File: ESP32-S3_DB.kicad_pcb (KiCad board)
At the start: 2 copper layers, 117 parts, among them CN1 JST_Battery, IC1 MAX485ESA+T, IC2 ATA6561-GAQW-N, J1 TYPE-C-31-M12_13, J10 Conn_01x16_Socket, J2 A - B, J3 H - L, J4 TYPE-C-31-M12_13, J5 EXT_LOAD, J6 R4_TX, J7 R4_RX, J8 Micro_SD_Card_Det1, J9 Conn_01x16_Socket, Q1 NMOS, Q2 NMOS, SW1 RESET, SW2 BOOT, SW3 ON/OFF, U1 ESP32-S3FH4R2, U3 IP5306, U4 CH340X, U5 AP2127N-3.3TRG1, X1 32.768KHz, Y1 40MHz

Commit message: Arranged power section on PCB
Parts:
- added D1: BLUE, ESP32-S3_Dev_Board:LED_0603_1608Metric, F.Cu at (160.5, 113.9)
- added R8: 0E, ESP32-S3_Dev_Board:R_0603_1608Metric, F.Cu at (150.2, 101.7)
- moved J4 329.5 mm to (170.6, 110.4), turned to 90 degrees
- moved R5 319.4 mm to (165.8, 94.0), turned to 90 degrees
- moved D11 313.2 mm to (164.0, 110.2), turned to 90 degrees
- moved D7 312.9 mm to (151.9, 120.7)
- moved R7 312.9 mm to (166.5, 107.8), turned to 90 degrees
- moved D3 312.6 mm to (151.8, 122.4), turned to 180 degrees
- moved R6 311.9 mm to (164.4, 112.5), turned to 180 degrees
- moved D9 311.2 mm to (151.8, 117.2)
- moved D8 311.0 mm to (151.8, 119.0), turned to 180 degrees
- moved R39 309.0 mm to (157.5, 114.0)
- moved R16 302.4 mm to (145.1, 126.2)
- moved R15 302.1 mm to (146.4, 104.4), turned to -90 degrees
- moved C10 296.3 mm to (146.0, 117.5)
- moved L4 295.6 mm to (139.6, 123.3), turned to 180 degrees
- moved R9 294.3 mm to (140.9, 116.8), turned to 180 degrees
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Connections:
- D2 pad 4: /INPUT POWER/5V -> /5V
- J1 pad A4: /INPUT POWER/5V -> /INPUT POWER/VIN
- J1 pad B4: /INPUT POWER/5V -> /INPUT POWER/VIN
- R15 pad 1: /INPUT POWER/5V -> /INPUT POWER/VIN
- R9 pad 1: /INPUT POWER/5V -> /INPUT POWER/VIN

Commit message: Added bulk Decoupling and arranged components
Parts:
- added C1: 22uF, ESP32-S3_Dev_Board:C_1206_3216Metric, F.Cu at (111.8, 120.4)
- added C37: 22uF, ESP32-S3_Dev_Board:C_1206_3216Metric, F.Cu at (111.8, 123.8)
- added C38: 22uF, ESP32-S3_Dev_Board:C_1206_3216Metric, F.Cu at (111.8, 127.1)
- added C39: 22uF, ESP32-S3_Dev_Board:C_1206_3216Metric, F.Cu at (111.8, 130.5)
- added R45: 10E, ESP32-S3_Dev_Board:R_0402_1005Metric, F.Cu at (131.6, 99.9)
- added R46: 10E, ESP32-S3_Dev_Board:R_0402_1005Metric, F.Cu at (135.2, 102.0)
- added R47: 10E, ESP32-S3_Dev_Board:R_0402_1005Metric, F.Cu at (-94.0, 66.7)
- added R48: 10E, ESP32-S3_Dev_Board:R_0402_1005Metric, F.Cu at (-94.0, 68.7)
- added R49: 10E, ESP32-S3_Dev_Board:R_0402_1005Metric, F.Cu at (-98.9, 66.7)
- added R50: 10E, ESP32-S3_Dev_Board:R_0402_1005Metric, F.Cu at (-98.9, 68.7)
- added R51: 10E, ESP32-S3_Dev_Board:R_0402_1005Metric, F.Cu at (-98.9, 70.7)
- added R52: 10E, ESP32-S3_Dev_Board:R_0402_1005Metric, F.Cu at (-98.9, 72.7)
- added R53: 10E, ESP32-S3_Dev_Board:R_0402_1005Metric, F.Cu at (-98.9, 74.7)
- added R54: 10E, ESP32-S3_Dev_Board:R_0402_1005Metric, F.Cu at (-98.9, 76.7)
- moved R26 311.1 mm to (167.2, 90.2), turned to 180 degrees
- moved R27 307.4 mm to (163.8, 90.3)
- moved J7 306.8 mm to (170.6, 73.9)
- moved J6 304.7 mm to (164.2, 74.1)
- moved J3 296.0 mm to (169.9, 121.9), turned to 180 degrees
- moved J2 291.8 mm to (170.0, 85.2)
- moved J8 286.6 mm to (151.3, 83.7)
- moved C20 282.9 mm to (153.7, 106.4), turned to 180 degrees
- moved C19 281.9 mm to (153.6, 111.4), turned to 180 degrees
- moved D10 280.8 mm to (138.6, 84.0)
- moved CN1 279.1 mm to (135.9, 127.8), turned to 180 degrees
- moved J5 276.4 mm to (129.7, 82.3)
- moved R20 272.5 mm to (149.4, 107.8)
- moved R43 272.1 mm to (144.3, 109.0)
- moved R44 269.6 mm to (144.5, 113.7)
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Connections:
- D13 pad 2: /BOOT_TXD -> Net-(D13-A)
- J1 pad A6: /D+ -> Net-(J1-D+-PadA6)
- J1 pad A7: /D- -> Net-(J1-D--PadA7)
- J1 pad B6: /D+ -> Net-(J1-D+-PadA6)
- J1 pad B7: /D- -> Net-(J1-D--PadA7)
- U1 pad 15: /SD_~{CS} -> Net-(U1-GPIO10)
- U1 pad 16: /SD_MOSI -> Net-(U1-GPIO11)
- U1 pad 17: /SD_CLK -> Net-(U1-GPIO12)
- U1 pad 18: /SD_MISO -> Net-(U1-GPIO13)
- U1 pad 25: /OTG_D- -> /ESP32-S3-MCU/D-
- U1 pad 26: /OTG_D+ -> /ESP32-S3-MCU/D+
- U4 pad 8: /BOOT_RXD -> Net-(U4-TXD)
- U4 pad 9: /BOOT_TXD -> Net-(D13-A)

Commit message: Changed USB C footprint and arranged components
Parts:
- added C40: 10uF, ESP32-S3_Dev_Board:C_0805_2012Metric, F.Cu at (202.4, 106.7)
- added C41: 1uF, ESP32-S3_Dev_Board:C_0603_1608Metric, F.Cu at (204.6, 106.7)
- J1, J4: footprint ESP32-S3_Dev_Board:USB-C_SMD-TYPE-C-31-M-12 -> ESP32-S3_Dev_Board:tyye_c_connector
- moved J9 301.7 mm to (131.2, 136.3), turned to -90 degrees
- moved R47 301.1 mm to (203.9, 110.5), turned to 180 degrees
- moved R48 301.0 mm to (203.9, 112.0), turned to 180 degrees
- moved J10 257.6 mm to (91.9, 138.8), turned to 90 degrees
- moved J6 66.4 mm to (230.5, 77.8)
- moved J2 62.8 mm to (230.8, 69.4)
- moved J8 60.7 mm to (210.7, 71.0)
- moved J3 56.8 mm to (192.3, 69.7), turned to 0 degrees
- moved J7 54.6 mm to (225.1, 77.8)
- moved J5 49.6 mm to (177.7, 69.8)
- moved J1 43.3 mm to (211.7, 110.5)
- moved J4 43.0 mm to (211.8, 122.8)
- moved R4 42.6 mm to (204.3, 113.7), turned to -90 degrees
- moved D11 41.8 mm to (203.8, 122.9)
- moved D2 37.1 mm to (198.0, 111.2)
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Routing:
- net Net-(J1-D--PadA7): track 0.00 -> 0.55 mm

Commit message: Placed RS-485, CAN Transceiver and battery charger
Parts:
- added TP1: RS_RX, ESP32-S3_Dev_Board:Test_Pad_1.5mm, F.Cu at (168.9, 121.2)
- added TP2: RS_TX, ESP32-S3_Dev_Board:Test_Pad_1.5mm, F.Cu at (172.7, 121.2)
- added TP3: CAN_TX, ESP32-S3_Dev_Board:Test_Pad_1.5mm, F.Cu at (143.2, 118.9)
- added TP4: CAN_RX, ESP32-S3_Dev_Board:Test_Pad_1.5mm, F.Cu at (147.0, 118.9)
- added TP5: GND, ESP32-S3_Dev_Board:Test_Pad_1.5mm, F.Cu at (170.8, 123.0)
- added TP6: GND, ESP32-S3_Dev_Board:Test_Pad_1.5mm, F.Cu at (150.7, 121.4)
- moved R33 313.2 mm to (174.3, 116.8), turned to 90 degrees
- moved R31 312.0 mm to (172.7, 117.8), turned to 90 degrees
- moved R28 311.8 mm to (168.1, 105.2)
- moved R29 308.6 mm to (170.8, 117.6), turned to 180 degrees
- moved R13 307.9 mm to (166.0, 107.8), turned to 90 degrees
- moved R30 307.2 mm to (168.9, 117.8), turned to 90 degrees
- moved R32 304.6 mm to (167.3, 116.8), turned to 90 degrees
- moved C22 301.7 mm to (167.4, 112.4), turned to -90 degrees
- moved R24 301.3 mm to (171.4, 107.2), turned to 90 degrees
- moved IC1 300.2 mm to (170.8, 112.5), turned to 90 degrees
- moved R25 299.9 mm to (170.2, 107.2), turned to 90 degrees
- moved D6 298.2 mm to (170.8, 101.1)
- moved SW2 279.2 mm to (196.3, 94.5)
- moved SW1 271.6 mm to (186.7, 94.5)
- moved R38 271.3 mm to (147.0, 116.1), turned to -90 degrees
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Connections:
- C22 pad 1: /3V3 -> Net-(IC1-VCC)
- C24 pad 2: /3V3 -> Net-(IC2-VCC)
- CN1 pad 1: /V_BAT -> GND
- CN1 pad 2: GND -> /V_BAT
- D12 pad 1: Net-(D12-K) -> GND
- D12 pad 2: /BOOT_RXD -> Net-(D12-A)
- D13 pad 1: Net-(D13-K) -> GND
- J2 pad 1: /RS-485_A -> /RS-485_B
- J2 pad 2: /RS-485_B -> /RS-485_A
- R13 pad 1: /3V3 -> Net-(IC1-VCC)
- R13 pad 2: Net-(IC1-VCC) -> /3V3
- R43 pad 1: GND -> Net-(D13-A)
- R43 pad 2: Net-(D13-K) -> Net-(U4-RXD)
- R44 pad 1: GND -> Net-(D12-A)
- R44 pad 2: Net-(D12-K) -> Net-(U4-TXD)
- R46 pad 1: Net-(D13-A) -> Net-(U4-RXD)
- U4 pad 9: Net-(D13-A) -> Net-(U4-RXD)
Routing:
- net unconnected-(J1-SBU2-PadB8): track 0.00 -> 0.55 mm
- net Net-(J1-D--PadA7): track 0.55 -> 0.00 mm

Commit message: Placed ESP32-S3
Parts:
- R2: value TBD -> 270
- moved C30 274.2 mm to (137.5, 109.5)
- moved C29 270.7 mm to (137.5, 108.0)
- moved R12 270.2 mm to (137.5, 111.0), turned to 180 degrees
- moved C21 254.2 mm to (196.7, 98.5)
- moved C18 244.7 mm to (187.3, 99.5)
- moved R51 240.0 mm to (135.5, 122.5), turned to 180 degrees
- moved R52 239.3 mm to (135.5, 121.2), turned to 180 degrees
- moved R53 238.7 mm to (135.5, 120.0), turned to 180 degrees
- moved R54 238.1 mm to (135.5, 118.8), turned to 180 degrees
- moved R2 210.3 mm to (123.2, 114.5), turned to 180 degrees
- moved R1 206.0 mm to (115.5, 124.8)
- moved R21 202.4 mm to (117.1, 126.1), turned to 90 degrees
- moved R8 70.6 mm to (203.8, 115.1)
- moved R45 64.1 mm to (187.1, 108.6)
- moved R46 60.5 mm to (187.1, 110.3)
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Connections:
- C29 pad 1: /3V3 -> /SD_CARD/VDD
- C30 pad 1: /3V3 -> /SD_CARD/VDD
- J8 pad 4: Net-(J8-VDD) -> /SD_CARD/VDD
- R12 pad 2: Net-(J8-VDD) -> /SD_CARD/VDD
- U1 pad 36: /ESP32-S3-MCU/GPIO 48 -> unconnected-(U1-SPICLK_N-Pad36)
- U1 pad 37: /ESP32-S3-MCU/GPIO 47 -> unconnected-(U1-SPICLK_P-Pad37)

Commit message: Placed all the components and added OSHW symbol
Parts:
- added D5: GREEN, ESP32-S3_Dev_Board:LED_0603_1608Metric, F.Cu at (112.5, 109.5)
- added R55: 500, ESP32-S3_Dev_Board:R_0402_1005Metric, F.Cu at (113.9, 109.5)
- moved R49 237.7 mm to (131.8, 123.9)
- moved R50 237.5 mm to (131.8, 125.0), turned to 180 degrees
- moved L3 207.5 mm to (117.0, 120.6)
- moved R17 185.0 mm to (111.8, 125.0), turned to 90 degrees
- moved C7 3.37 mm to (115.8, 117.4)
- moved L2 3.37 mm to (114.0, 116.9)
- moved C5 3.37 mm to (112.2, 117.4)
- moved C2 1.75 mm to (111.9, 121.2)
- moved C3 1.75 mm to (113.8, 121.1)
- moved C6 1.65 mm to (115.3, 121.1)
- moved C8 0.66 mm to (118.7, 120.9)

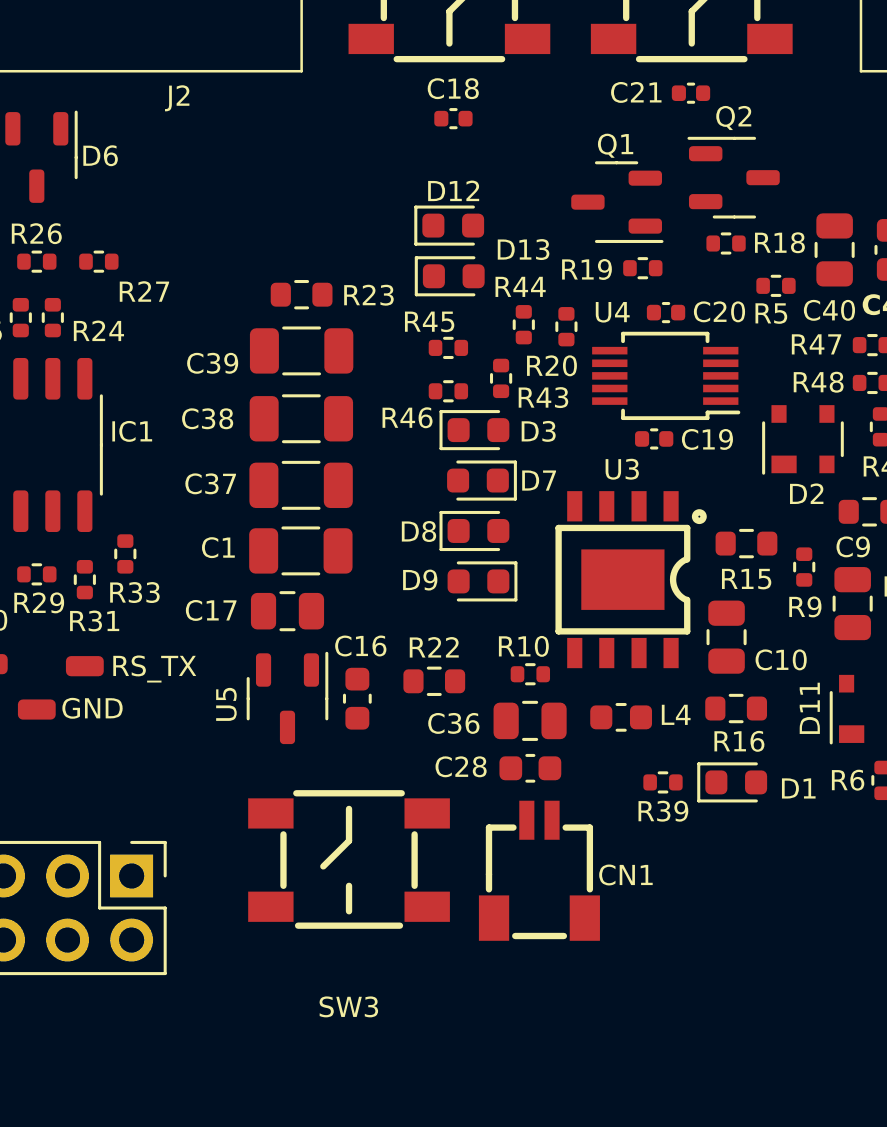
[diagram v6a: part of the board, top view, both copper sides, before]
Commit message: Corrected schematic to PCB export error and warings and IP5306 and SD card section
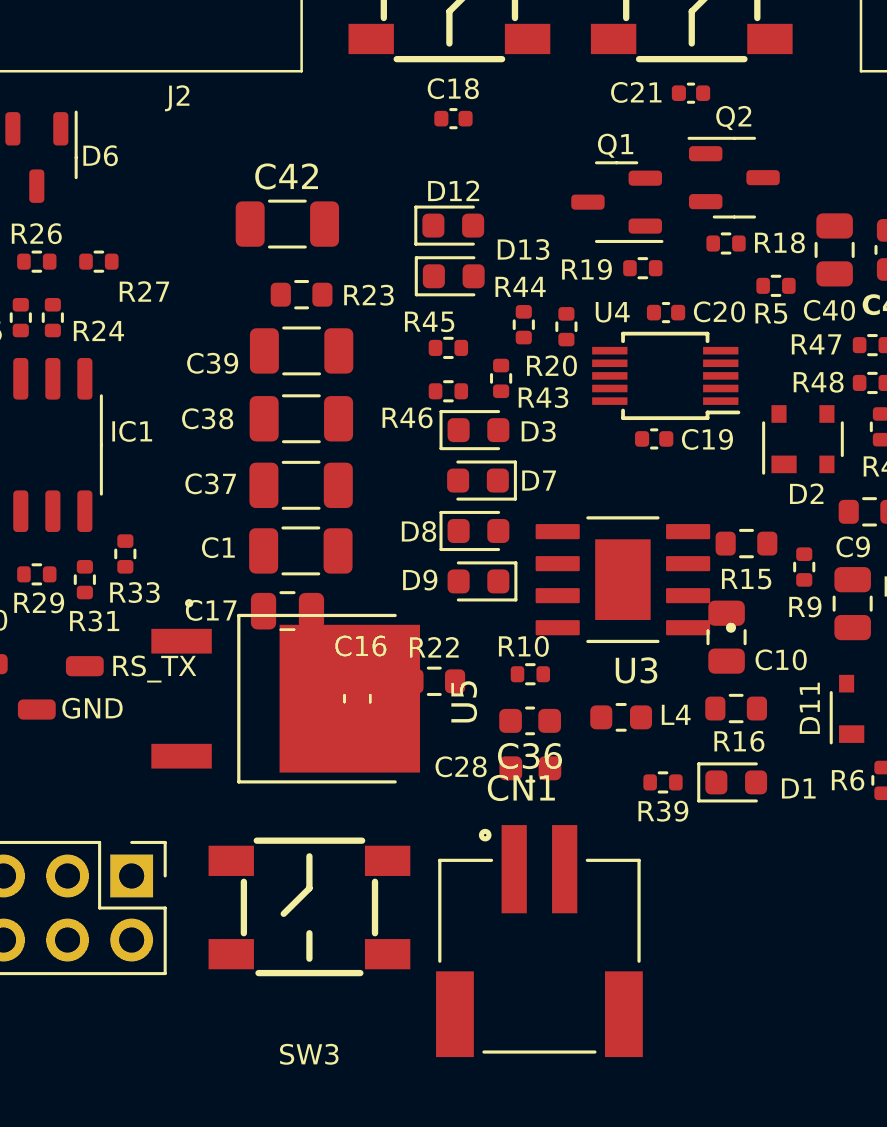
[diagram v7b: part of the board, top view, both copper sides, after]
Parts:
- added C42: 22uF, ESP32-S3_Dev_Board:C_1206_3216Metric, F.Cu at (180.7, 103.7)
- AE1: value Antenna -> Antenna_Shield
- C36: value 10uF -> 22uF; footprint ESP32-S3_Dev_Board:C_0805_2012Metric -> ESP32-S3_Dev_Board:C_0603_1608Metric
- CN1: footprint ESP32-S3_Dev_Board:CONN-SMD_2P-P1.00_SM02B-SRSS-TB-LF-SN -> ESP32-S3_Dev_Board:JST_2mm
- U3: footprint ESP32-S3_Dev_Board:ESOP-8_L4.9-W3.9-P1.27-LS6.0-BL-EP -> ESP32-S3_Dev_Board:ESOP-8
- U5: value AP2127N-3.3TRG1 -> LD1117DT33CTR; footprint ESP32-S3_Dev_Board:SOT-23-3 -> ESP32-S3_Dev_Board:DPAK
- moved SW3 2.45 mm to (181.6, 130.8)
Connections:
- AE1 pad 2: (no net) -> GND
- C1 pad 1: Net-(U5-VOUT) -> /5V
- C36 pad 1: /V_BAT -> Net-(U3-BAT)
- C37 pad 1: Net-(U5-VOUT) -> /5V
- C38 pad 1: Net-(U5-VOUT) -> /5V
- C39 pad 1: Net-(U5-VOUT) -> /5V
- D2 pad 4: /5V -> /INPUT POWER/VIN

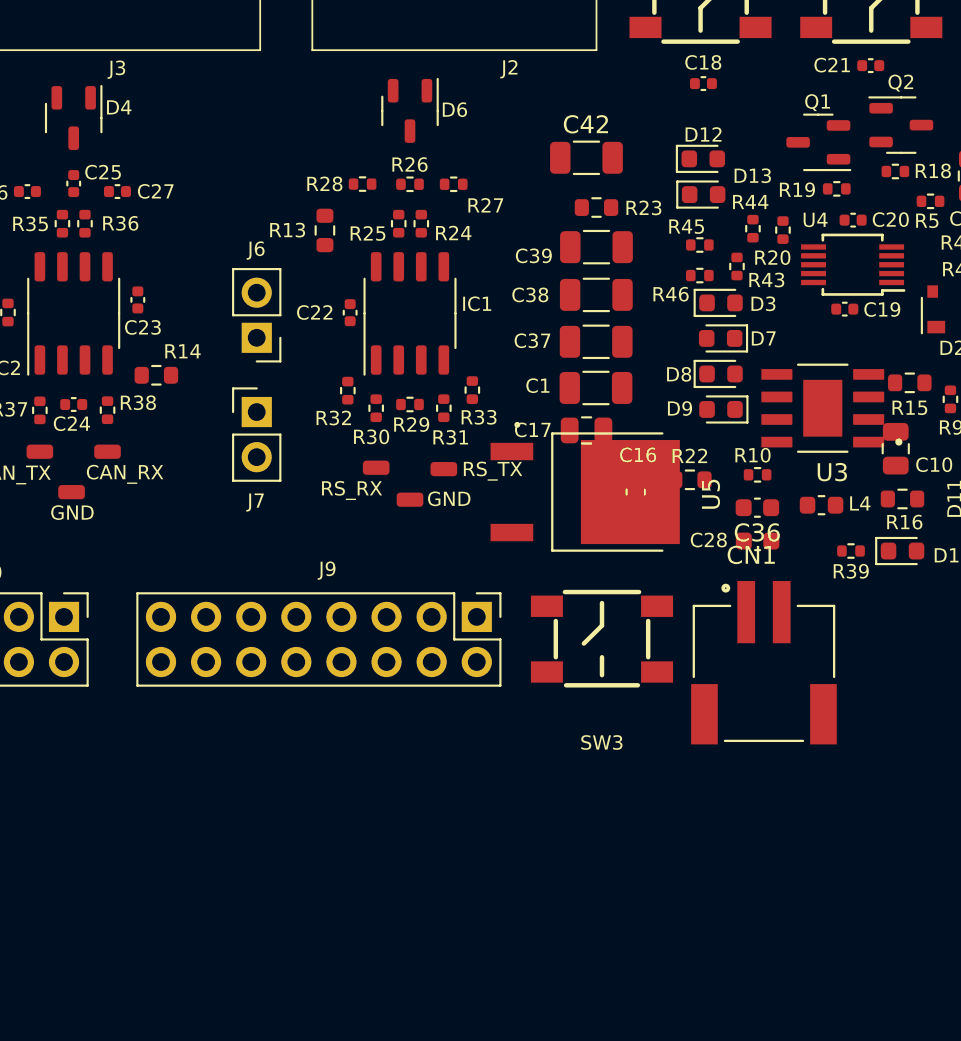
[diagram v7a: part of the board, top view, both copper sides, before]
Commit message: Added CAN Jumpers, changed jumper pitch to 1.27mm
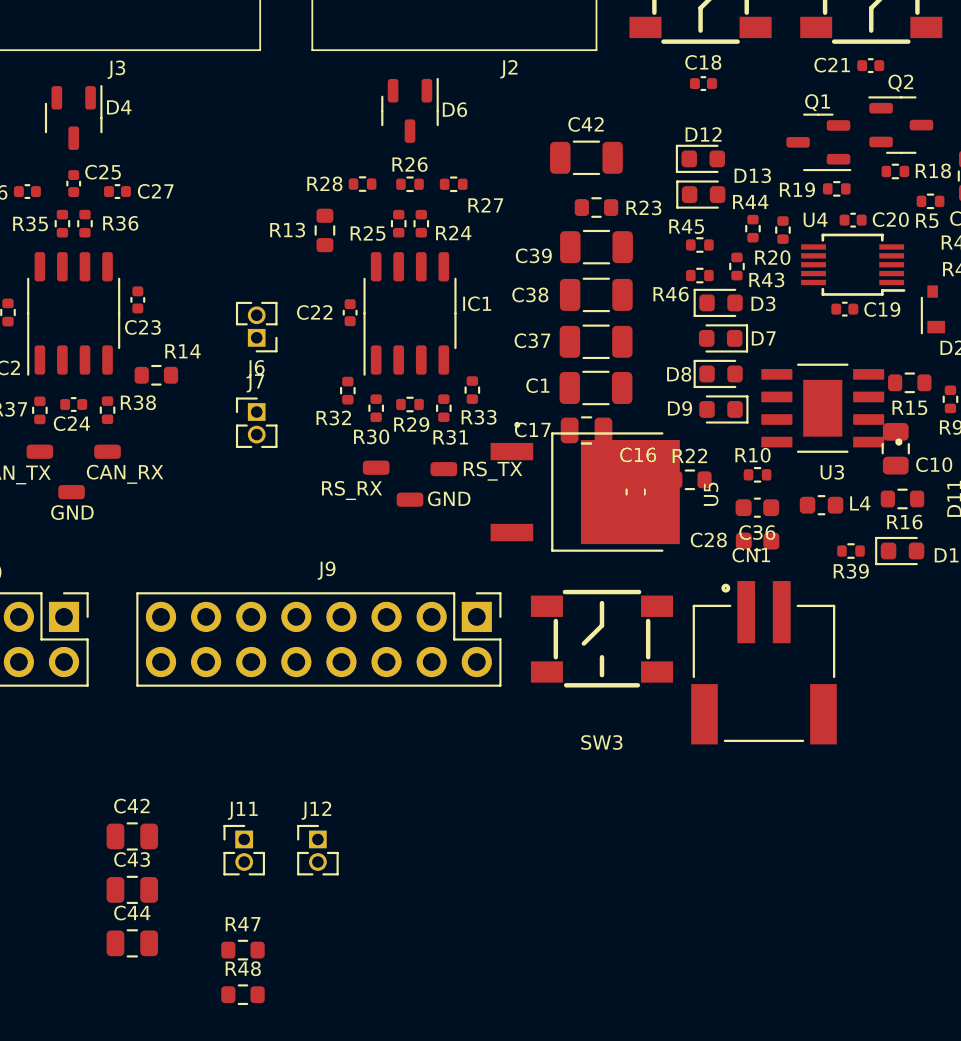
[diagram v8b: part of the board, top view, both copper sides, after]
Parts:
- added C42: 10uF, ESP32-S3_Dev_Board:C_0805_2012Metric, F.Cu at (155.2, 141.9)
- added C43: 10uF, ESP32-S3_Dev_Board:C_0805_2012Metric, F.Cu at (155.2, 144.9)
- added C44: 10uF, ESP32-S3_Dev_Board:C_0805_2012Metric, F.Cu at (155.2, 147.9)
- added J11: CAN_TX, ESP32-S3_Dev_Board:PinHeader_1x02_P1.27mm_Vertical, F.Cu at (161.5, 142.1)
- added J12: CAN_RX, ESP32-S3_Dev_Board:PinHeader_1x02_P1.27mm_Vertical, F.Cu at (165.6, 142.1)
- added R47: 0E, ESP32-S3_Dev_Board:R_0603_1608Metric, F.Cu at (161.4, 148.3)
- added R48: 0E, ESP32-S3_Dev_Board:R_0603_1608Metric, F.Cu at (161.4, 150.8)
- IC1: value MAX485ESA+T -> SP3071EEN-L/TR
- J6, J7: footprint ESP32-S3_Dev_Board:PinHeader_1x02_P2.54mm_Vertical -> ESP32-S3_Dev_Board:PinHeader_1x02_P1.27mm_Vertical
- R35: value 59 -> 59E
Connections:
- net /BOOT_RXD renamed /U2U_TXD
- net /BOOT_TXD renamed /U2U_RXD
- net /RS-485/A renamed /RS_485/RS485_A
- net /RS-485/B renamed /RS_485/RS485_B
- net /RS-485/RS-485_DI renamed /RS_485/RS-485_DI
- net /RS-485/RS-485_RO renamed /RS_485/RS-485_RO
- net /RS-485_A renamed /RS_485_A
- net /RS-485_B renamed /RS_485_B
- net /RS-485_RX renamed /RS-485_RX/GPIO46
- net /RS-485_TX renamed /RS-485_TX/GPIO45
- D10 pad 1: /SD_CARD/SD_CS -> /~{MCU_SL_CS}
- D10 pad 3: /SD_MOSI -> /MCU_SL_MOSI
- D10 pad 4: /3V3 -> /SD_CARD/VDD
- D10 pad 5: /SD_CLK -> /MCU_SL_CLK
- D10 pad 6: /SD_MISO -> /MCU_SL_MISO
- J8 pad 2: /SD_~{CS} -> /~{MCU_SL_CS}
- J8 pad 3: /SD_MOSI -> /MCU_SL_MOSI
- J8 pad 5: /SD_CLK -> /MCU_SL_CLK
- J8 pad 7: /SD_MISO -> /MCU_SL_MISO
- J9 pad 13: /CAN_TXD -> /CAN_TXD/GPIO7
- J9 pad 14: /CAN_RXD -> /CAN_RXD/GPIO8
- R11 pad 1: /SD_MISO -> /~{MCU_SL_CS}
- R37 pad 2: /CAN_TXD -> /CAN_TRANS_TXD
- R38 pad 2: /CAN_RXD -> /CAN_TRANS_RXD
- R40 pad 1: /SD_MOSI -> /MCU_SL_CLK
- R41 pad 1: /SD_CLK -> /MCU_SL_MISO
- R42 pad 1: /SD_~{CS} -> /MCU_SL_MOSI
- R51 pad 1: /SD_~{CS} -> /~{MCU_SL_CS}
- R52 pad 1: /SD_MOSI -> /MCU_SL_MISO
- R53 pad 1: /SD_CLK -> /MCU_SL_CLK
- R54 pad 1: /SD_MISO -> /MCU_SL_MOSI
- TP3 pad 1: /CAN_TXD -> /CAN_TRANS_TXD
- TP4 pad 1: /CAN_RXD -> /CAN_TRANS_RXD
- U1 pad 12: /CAN_TXD -> /CAN_TXD/GPIO7
- U1 pad 13: /CAN_RXD -> /CAN_RXD/GPIO8
